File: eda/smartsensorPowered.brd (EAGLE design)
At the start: 47 x 26.7 mm, 38 parts, among them Q1 IRFML8244, Q2 IRFML8244, Q3 IRFML8244, Q4 IRFML8244, U1 ISL83491SOIC, U2 ATTINY1634

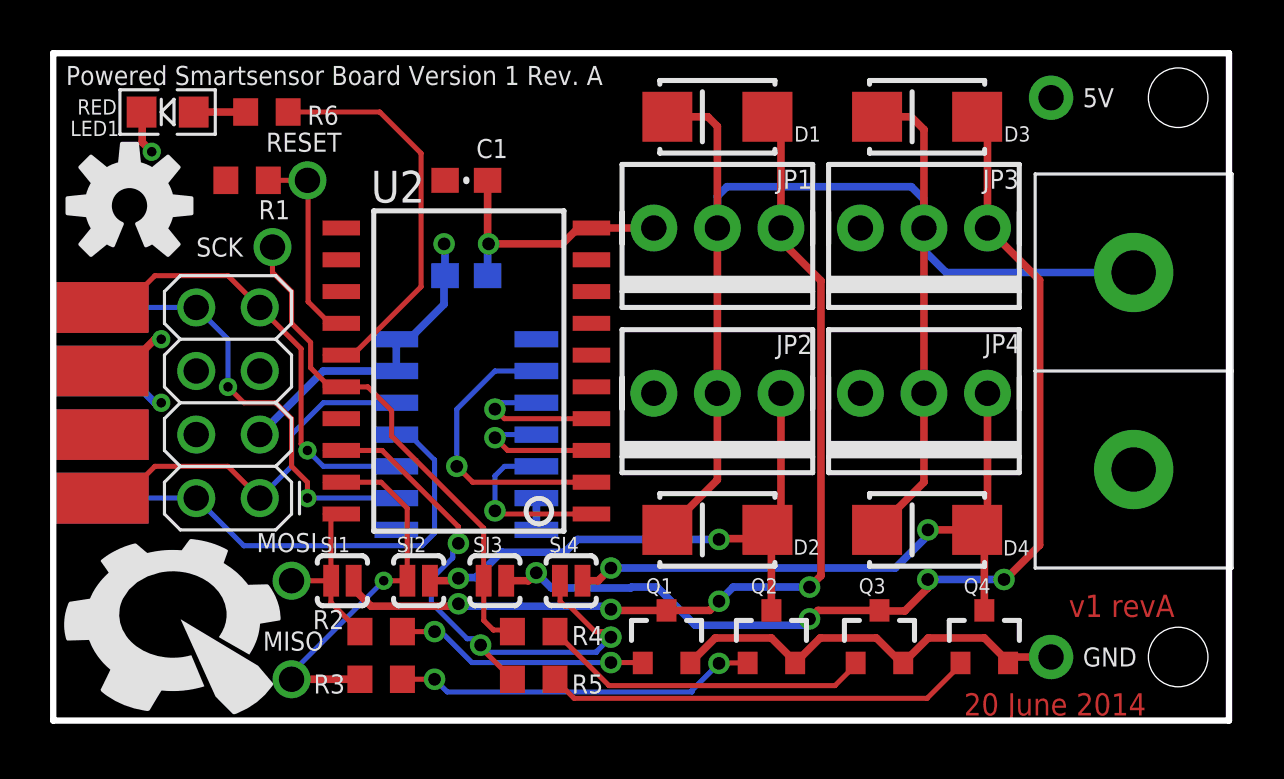
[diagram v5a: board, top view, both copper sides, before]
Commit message: Added smartsensor variation checkboxes.
On smartsensor.brd and smartsensorPowered.brd.
Minor via shifting to accomodate text.
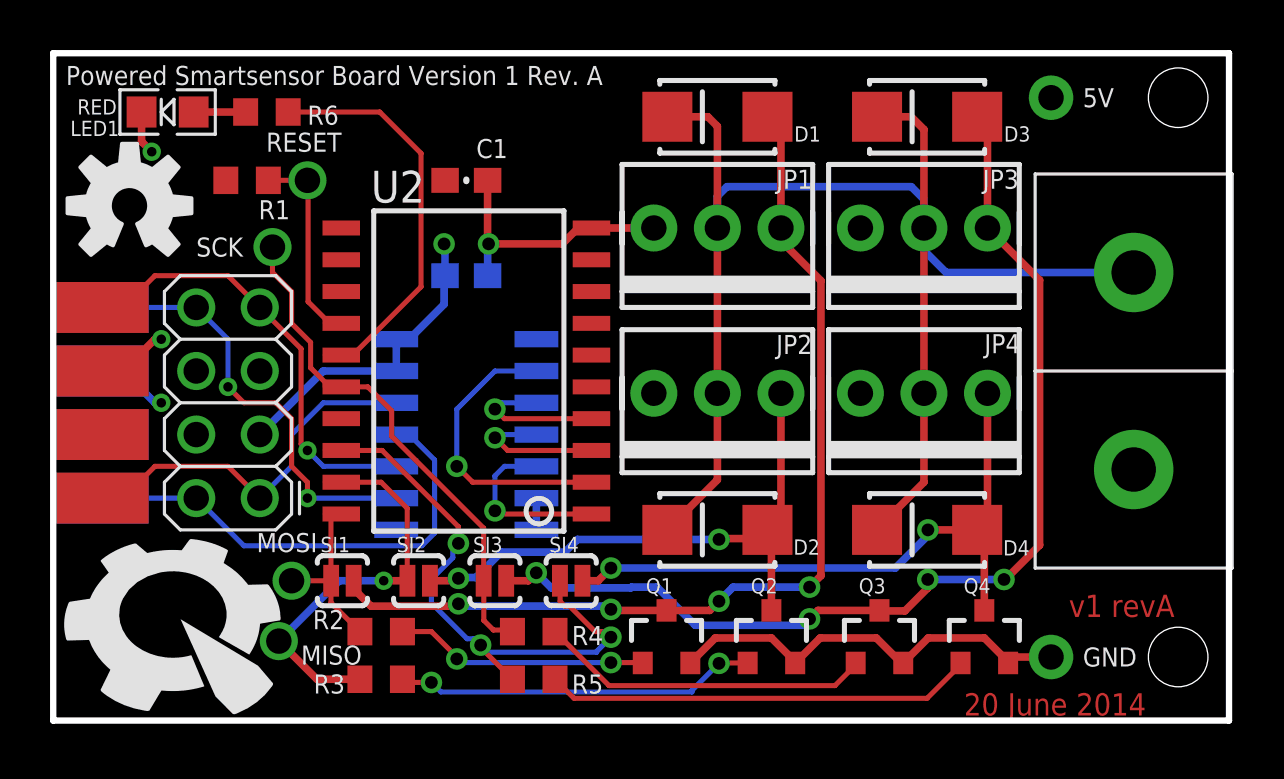
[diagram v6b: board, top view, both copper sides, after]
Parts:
- moved MISO 1.61 mm to (9.02, 3.17)
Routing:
- net IO2: track 15.7 -> 16.6 mm
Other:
- board text added: "SENSOR VARIANT"
- board text added: "SERVO"
- board text added: "SOLENOID"
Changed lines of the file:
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@@
 <layer number="49" name="Reference" color="7" fill="1" visible="yes" active="yes"/>
 <layer number="50" name="dxf" color="7" fill="1" visible="no" active="no"/>
-<layer number="51" name="tDocu" color="6" fill="1" visible="no" active="yes"/>
-<layer number="52" name="bDocu" color="6" fill="1" visible="no" active="yes"/>
+<layer number="51" name="tDocu" color="6" fill="1" visible="yes" active="yes"/>
+<layer number="52" name="bDocu" color="6" fill="1" visible="yes" active="yes"/>
 <layer number="53" name="tGND_GNDA" color="7" fill="9" visible="no" active="no"/>
 <layer number="54" name="bGND_GNDA" color="1" fill="9" visible="no" active="no"/>
@@
 <text x="40.5892" y="4.1402" size="0.889" layer="1" font="vector" ratio="20">v1 revA</text>
 <text x="39.37" y="8.89" size="0.762" layer="22" font="vector" ratio="20" rot="MR0">(c) Pioneers in Engineering</text>
+<rectangle x1="17.526" y1="0.889" x2="18.796" y2="2.159" layer="22"/>
+<text x="17.145" y="0.889" size="1.27" layer="22" font="vector" ratio="15" rot="MR0">SERVO</text>
+<rectangle x1="9.906" y1="0.889" x2="11.176" y2="2.159" layer="22"/>
+<text x="9.525" y="0.889" size="1.27" layer="22" font="vector" ratio="15" rot="MR0">SOLENOID</text>
+<text x="16.51" y="2.794" size="1.27" layer="22" font="vector" ratio="15" rot="MR0">SENSOR VARIANT</text>
+<wire x1="16.891" y1="2.54" x2="0.508" y2="2.54" width="0.2032" layer="22"/>
+<wire x1="0.508" y1="2.54" x2="0.508" y2="0.508" width="0.2032" layer="22"/>
+<wire x1="0.508" y1="0.508" x2="19.177" y2="0.508" width="0.2032" layer="22"/>
+<wire x1="19.177" y1="0.508" x2="19.177" y2="2.54" width="0.2032" layer="22"/>
+<wire x1="19.177" y1="2.54" x2="16.891" y2="2.54" width="0.2032" layer="22"/>
+<wire x1="16.891" y1="2.54" x2="16.891" y2="4.445" width="0.2032" layer="22"/>
+<wire x1="16.891" y1="4.445" x2="0.508" y2="4.445" width="0.2032" layer="22"/>
+<wire x1="0.508" y1="4.445" x2="0.508" y2="2.54" width="0.2032" layer="22"/>
 </plain>
 <attributes>
@@
 <attribute name="VALUE" x="8.255" y="3.048" size="1.27" layer="27" font="vector"/>
 </element>
-<element name="MISO" library="pie" package="POGO_PIN_394" value="" x="9.525" y="1.651" smashed="yes">
-<attribute name="PIE-INT-REF-NUM" value="POGO-PIN" x="9.525" y="1.651" size="1.778" layer="27" display="off"/>
-<attribute name="NAME" x="8.382" y="2.794" size="0.762" layer="25" font="vector" ratio="15"/>
-<attribute name="VALUE" x="8.255" y="-0.889" size="1.27" layer="27" font="vector"/>
+<element name="MISO" library="pie" package="POGO_PIN_394" value="" x="9.017" y="3.175" smashed="yes">
+<attribute name="PIE-INT-REF-NUM" value="POGO-PIN" x="9.017" y="3.175" size="1.778" layer="27" display="off"/>
+<attribute name="NAME" x="9.906" y="2.2352" size="0.762" layer="25" font="vector" ratio="15"/>
+<attribute name="VALUE" x="7.747" y="0.635" size="1.27" layer="27" font="vector"/>
 </element>
 <element name="SCK" library="pie" package="POGO_PIN_394" value="" x="8.763" y="18.923" smashed="yes">
@@
 <contactref element="U$12" pad="5"/>
 <contactref element="U$12" pad="4"/>
-<wire x1="3.937" y1="22.733" x2="3.556" y2="23.114" width="0.3048" layer="1"/>
-<wire x1="3.556" y1="23.114" x2="3.556" y2="24.2951" width="0.3048" layer="1"/>
 <wire x1="3.556" y1="24.2951" x2="3.5306" y2="24.3205" width="0.3048" layer="1"/>
 <contactref element="U$13" pad="5"/>
@@
 <wire x1="4.064" y1="15.24" x2="4.318" y2="15.24" width="0.3048" layer="1"/>
 <via x="4.318" y="15.24" extent="1-16" drill="0.381"/>
+<wire x1="3.5306" y1="24.3205" x2="3.5306" y2="23.1394" width="0.3048" layer="1"/>
+<wire x1="3.5306" y1="23.1394" x2="3.937" y2="22.733" width="0.3048" layer="1"/>
 </signal>
 <signal name="TX">
@@
 <wire x1="10.875" y1="15.875" x2="11.049" y2="15.875" width="0.2032" layer="1"/>
 <wire x1="11.049" y1="15.875" x2="10.1854" y2="16.7386" width="0.2032" layer="1"/>
-<wire x1="10.1854" y1="16.7386" x2="10.1854" y2="21.5646" width="0.2032" layer="1"/>
 <wire x1="11.51" y1="15.875" x2="11.049" y2="15.875" width="0.2032" layer="1"/>
 <contactref element="RESET" pad="POGO_PIN"/>
-<wire x1="8.597" y1="21.59" x2="10.16" y2="21.59" width="0.2032" layer="1"/>
-<wire x1="10.1854" y1="21.5646" x2="10.16" y2="21.59" width="0" layer="19" extent="1-1"/>
+<wire x1="10.1854" y1="16.7386" x2="10.1854" y2="21.5646" width="0.2032" layer="1"/>
+<wire x1="10.1854" y1="21.5646" x2="10.16" y2="21.59" width="0.2032" layer="1"/>
+<wire x1="10.16" y1="21.59" x2="8.597" y2="21.59" width="0.2032" layer="1"/>
 </signal>
 <signal name="A_P">
@@
 <wire x1="14.1478" y1="8.4836" x2="14.1478" y2="5.5952" width="0.2032" layer="1"/>
 <wire x1="14.1478" y1="5.5952" x2="14.155" y2="5.588" width="0.2032" layer="1"/>
-<wire x1="12.2564" y1="1.651" x2="9.525" y2="1.651" width="0.3048" layer="1"/>
 <via x="13.208" y="5.588" extent="1-16" drill="0.381"/>
-<wire x1="14.155" y1="5.588" x2="13.208" y2="5.588" width="0.2032" layer="1"/>
+<wire x1="14.155" y1="5.588" x2="13.208" y2="5.588" width="0.3048" layer="1"/>
 <wire x1="10.875" y1="9.525" x2="11.51" y2="9.525" width="0.2032" layer="1"/>
 <contactref element="MISO" pad="POGO_PIN"/>
-<wire x1="9.525" y1="1.651" x2="9.525" y2="1.905" width="0.2032" layer="16"/>
-<wire x1="9.525" y1="1.905" x2="13.208" y2="5.588" width="0.2032" layer="16"/>
+<wire x1="12.2564" y1="1.651" x2="10.541" y2="1.651" width="0.3048" layer="1"/>
+<wire x1="10.541" y1="1.651" x2="9.017" y2="3.175" width="0.3048" layer="1"/>
+<wire x1="13.208" y1="5.588" x2="11.43" y2="5.588" width="0.3048" layer="16"/>
+<wire x1="11.43" y1="5.588" x2="9.017" y2="3.175" width="0.3048" layer="16"/>
 </signal>
 <signal name="IO3">
@@
 <contactref element="R2" pad="2"/>
 <wire x1="23.418" y1="2.159" x2="23.561" y2="2.302" width="0.3048" layer="1"/>
-<wire x1="13.9564" y1="3.556" x2="15.24" y2="3.556" width="0.2032" layer="1"/>
-<via x="15.24" y="3.556" extent="1-16" drill="0.508"/>
-<wire x1="15.24" y1="3.556" x2="15.494" y2="3.556" width="0.2032" layer="16"/>
-<wire x1="15.494" y1="3.556" x2="16.73225" y2="2.31775" width="0.2032" layer="16"/>
+<via x="16.129" y="2.4638" extent="1-16" drill="0.508"/>
 <via x="22.2885" y="2.31775" extent="1-16" drill="0.508"/>
 <wire x1="23.545" y1="2.286" x2="23.561" y2="2.302" width="0.2032" layer="1"/>
-<wire x1="16.73225" y1="2.31775" x2="22.2885" y2="2.31775" width="0.2032" layer="16"/>
+<wire x1="16.27505" y1="2.31775" x2="22.2885" y2="2.31775" width="0.2032" layer="16"/>
 <wire x1="22.2885" y1="2.31775" x2="23.54525" y2="2.31775" width="0.2032" layer="1"/>
 <wire x1="23.54525" y1="2.31775" x2="23.561" y2="2.302" width="0.2032" layer="1"/>
+<wire x1="16.27505" y1="2.31775" x2="16.129" y2="2.4638" width="0.2032" layer="16"/>
+<wire x1="16.129" y1="2.4638" x2="16.129" y2="2.54" width="0.2032" layer="1"/>
+<wire x1="16.129" y1="2.54" x2="15.113" y2="3.556" width="0.2032" layer="1"/>
+<wire x1="15.113" y1="3.556" x2="13.9564" y2="3.556" width="0.2032" layer="1"/>
 </signal>
 <signal name="N$4">
@@
 <contactref element="R3" pad="2"/>
 <via x="26.6065" y="2.286" extent="1-16" drill="0.508"/>
-<wire x1="25.527" y1="1.143" x2="15.748" y2="1.143" width="0.2032" layer="16"/>
-<wire x1="15.748" y1="1.143" x2="15.24" y2="1.651" width="0.2032" layer="16"/>
-<via x="15.24" y="1.651" extent="1-16" drill="0.508"/>
-<wire x1="15.24" y1="1.651" x2="13.9564" y2="1.651" width="0.2032" layer="1"/>
+<wire x1="25.527" y1="1.143" x2="15.494" y2="1.143" width="0.2032" layer="16"/>
+<via x="15.113" y="1.524" extent="1-16" drill="0.508"/>
 <wire x1="25.527" y1="1.143" x2="25.527" y2="1.2065" width="0.2032" layer="16"/>
 <wire x1="25.527" y1="1.2065" x2="26.6065" y2="2.286" width="0.2032" layer="16"/>
 <wire x1="27.752" y1="2.302" x2="26.6225" y2="2.302" width="0.2032" layer="1"/>
 <wire x1="26.6225" y1="2.302" x2="26.6065" y2="2.286" width="0.2032" layer="1"/>
+<wire x1="15.494" y1="1.143" x2="15.113" y2="1.524" width="0.2032" layer="16"/>
+<wire x1="15.113" y1="1.524" x2="14.0834" y2="1.524" width="0.2032" layer="1"/>
+<wire x1="14.0834" y1="1.524" x2="13.9564" y2="1.651" width="0.2032" layer="1"/>
 </signal>
 <signal name="N$7">

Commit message: Standardized copyright and "Design by" info among boards.
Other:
- board text added: "(c) Pioneers in Engineering. Design by: Vincent Donato and Devin He. This design is open source hardware. For more information, visit pioneers.berkeley.edu/opensource."
- board text removed: "(c) Pioneers in Engineering"
- board text removed: "Design by: Vincent Donato and Devin He This design is open source hardware. For more information, visit pioneers.berkeley.edu/opensource"
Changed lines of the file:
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@@
 <wire x1="0" y1="26.67" x2="0" y2="0" width="0.254" layer="20"/>
 <text x="36.3982" y="0.2032" size="0.889" layer="1" font="vector" ratio="20">20 June 2014</text>
-<text x="38.354" y="0.889" size="0.6096" layer="22" ratio="20" rot="MR0">Design by:
- Vincent Donato and     Devin He
+<text x="38.354" y="20.828" size="0.762" layer="22" font="vector" ratio="20" rot="MR0">(c) Pioneers in Engineering.
+Design by: Vincent Donato and Devin He.
 This design is open source hardware.
 For more information, visit
-pioneers.berkeley.edu/opensource</text>
+pioneers.berkeley.edu/opensource.</text>
 <text x="0.508" y="25.4" size="0.762" layer="21" ratio="15">Powered Smartsensor Board Version 1 Rev. A</text>
 <text x="40.5892" y="4.1402" size="0.889" layer="1" font="vector" ratio="20">v1 revA</text>
-<text x="39.37" y="8.89" size="0.762" layer="22" font="vector" ratio="20" rot="MR0">(c) Pioneers in Engineering</text>
 <rectangle x1="17.526" y1="0.889" x2="18.796" y2="2.159" layer="22"/>
 <text x="17.145" y="0.889" size="1.27" layer="22" font="vector" ratio="15" rot="MR0">SERVO</text>
